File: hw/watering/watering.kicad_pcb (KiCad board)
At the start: 2 copper layers, 57 x 57 mm, 51 parts, among them J2 USB_C_Receptacle, SW1 KMS221GLFS, SW2 KMS221GLFS, U1 ESP32-C6, U2 DRV8220DSG, U3 NCP163AFCT330T2G, U4 STI3508, U5 STI3508, U6 STI3508, Y1 40MHz, Y2 32768Hz

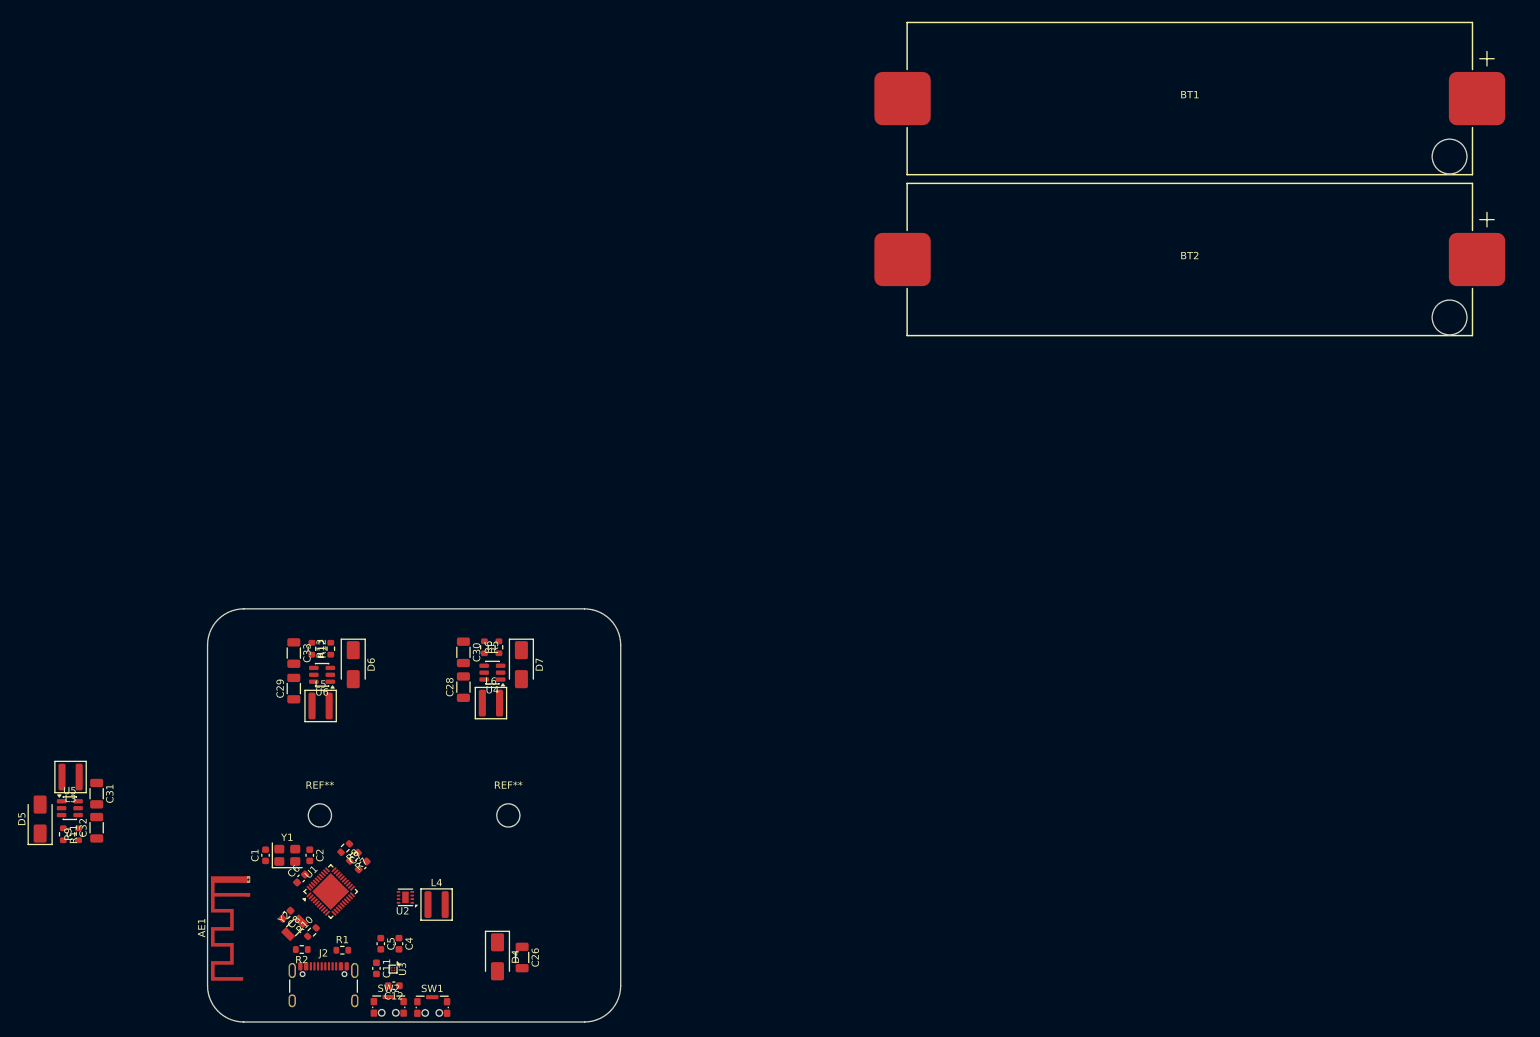
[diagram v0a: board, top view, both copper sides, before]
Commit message: connections completet. started placing and routing
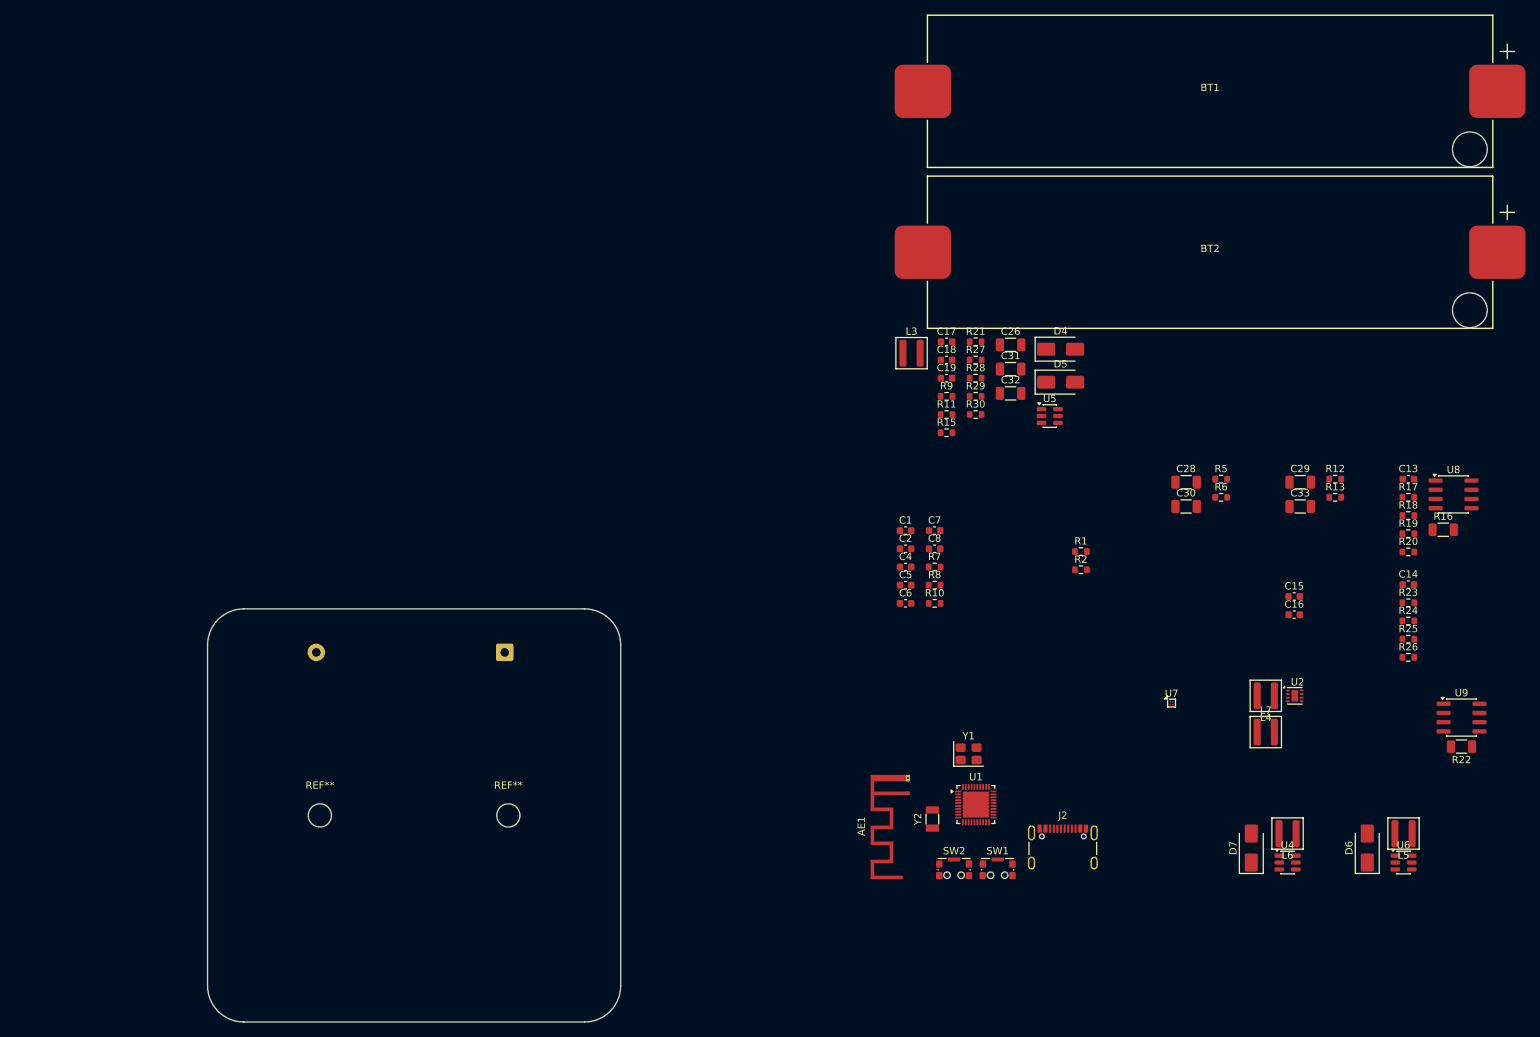
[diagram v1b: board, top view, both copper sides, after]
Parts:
- removed C11, C12: 1u, Capacitor_SMD:C_0603_1608Metric
- removed U3: NCP163AFCT330T2G, Package_CSP:WLCSP-4_0.64x0.64mm_Layout2x2_P0.35mm
- added C13: 1u, Capacitor_SMD:C_0603_1608Metric, F.Cu at (265.7, 82.1)
- added C14: 1u, Capacitor_SMD:C_0603_1608Metric, F.Cu at (265.7, 96.7)
- added C15: 1u, Capacitor_SMD:C_0603_1608Metric, F.Cu at (249.9, 98.3)
- added C16: 1u, Capacitor_SMD:C_0603_1608Metric, F.Cu at (249.9, 100.8)
- added C17: 1u, Capacitor_SMD:C_0603_1608Metric, F.Cu at (202.0, 63.2)
- added C18: 1u, Capacitor_SMD:C_0603_1608Metric, F.Cu at (202.0, 65.7)
- added C19: 1u, Capacitor_SMD:C_0603_1608Metric, F.Cu at (202.0, 68.2)
- added L7: 22u, Inductor_SMD:L_Wuerth_MAPI-4030, F.Cu at (246.0, 117.0)
- added R15: 10k, Resistor_SMD:R_0603_1608Metric, F.Cu at (202.0, 75.7)
- added R16: 0R1, Resistor_SMD:R_1206_3216Metric, F.Cu at (270.5, 89.1)
- added R17: 10k, Resistor_SMD:R_0603_1608Metric, F.Cu at (265.7, 84.6)
- added R18: 10k, Resistor_SMD:R_0603_1608Metric, F.Cu at (265.7, 87.1)
- added R19: 100k, Resistor_SMD:R_0603_1608Metric, F.Cu at (265.7, 89.6)
- added R20: 10k, Resistor_SMD:R_0603_1608Metric, F.Cu at (265.7, 92.1)
- added R21: 39k, Resistor_SMD:R_0603_1608Metric, F.Cu at (206.0, 63.2)
- added R22: 0R1, Resistor_SMD:R_1206_3216Metric, F.Cu at (273.0, 119.0)
- added R23: 10k, Resistor_SMD:R_0603_1608Metric, F.Cu at (265.7, 99.2)
- added R24: 10k, Resistor_SMD:R_0603_1608Metric, F.Cu at (265.7, 101.7)
- added R25: 10k, Resistor_SMD:R_0603_1608Metric, F.Cu at (265.7, 104.2)
- added R26: 100k, Resistor_SMD:R_0603_1608Metric, F.Cu at (265.7, 106.7)
- added R27: 220k, Resistor_SMD:R_0603_1608Metric, F.Cu at (206.0, 65.7)
- added R28: 10k, Resistor_SMD:R_0603_1608Metric, F.Cu at (206.0, 68.2)
- added R29: 47k, Resistor_SMD:R_0603_1608Metric, F.Cu at (206.0, 70.7)
- added R30: 10k, Resistor_SMD:R_0603_1608Metric, F.Cu at (206.0, 73.2)
- added SC1: Solar_Cell, Capacitor_THT:CP_Axial_L20.0mm_D10.0mm_P26.00mm_Horizontal, B.Cu at (141.0, 106.0)
- added U7: NCP163AFCT330T2G, Package_CSP:WLCSP-4_0.64x0.64mm_Layout2x2_P0.35mm, F.Cu at (233.0, 113.0)
- added U8: MCP6002-xSN, Package_SO:SOIC-8_3.9x4.9mm_P1.27mm, F.Cu at (271.9, 84.2)
- added U9: MCP6002-xSN, Package_SO:SOIC-8_3.9x4.9mm_P1.27mm, F.Cu at (273.0, 115.0)
- moved D5 153.1 mm to (217.7, 68.7), turned to 0 degrees
- moved U6 151.4 mm to (265.0, 135.0), turned to 0 degrees
- moved L5 150.4 mm to (265.0, 131.0), turned to 180 degrees
- moved U5 145.6 mm to (216.2, 73.4)
- moved R12 143.1 mm to (255.6, 82.1), turned to 0 degrees
- moved D6 142.2 mm to (260.0, 133.0), turned to 90 degrees
- moved C29 141.7 mm to (250.7, 82.5), turned to 0 degrees
- moved C33 140.3 mm to (250.7, 85.9), turned to 0 degrees
- moved R13 140.1 mm to (255.6, 84.6), turned to 0 degrees
- moved C32 139.6 mm to (210.8, 70.3), turned to 0 degrees
- moved C31 139.0 mm to (210.8, 66.9), turned to 0 degrees
- moved R11 134.9 mm to (202.0, 73.2), turned to 0 degrees
- moved R9 134.1 mm to (202.0, 70.7), turned to 0 degrees
- moved L3 129.9 mm to (197.1, 64.7), turned to 0 degrees
- moved U2 125.8 mm to (250.0, 112.0), turned to 0 degrees
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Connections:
- net /controller/bat_interrupt renamed /controller/i_usb_meas
- L4 pad 2: /solar/V_bat -> /solar/current_meas/i_in
- U1 pad 10: unconnected-(U1-MTMS/GPIO4/FSPIHD/ADC1_CH4-Pad10) -> /controller/V_solar_meas
- U1 pad 11: unconnected-(U1-MTDI/GPIO5/FSPIWP/ADC1_CH5-Pad11) -> /controller/V_usb_meas
- U1 pad 12: unconnected-(U1-MTCK/GPIO6/FSPICLK/ADC1_CH6-Pad12) -> /controller/V_bat_meas
- U1 pad 14: unconnected-(U1-GPIO8-Pad14) -> /controller/pwm-enable
- U1 pad 15: unconnected-(U1-GPIO9-Pad15) -> /controller/usb-pwm
- U1 pad 16: unconnected-(U1-GPIO10-Pad16) -> /controller/solar-pwm
- U1 pad 9: unconnected-(U1-GPIO3/ADC1_CH3-Pad9) -> /controller/i_meas_solar
- U2 pad 3: Net-(U2-OUT1) -> Net-(U2-OUT2)
- U2 pad 5: /solar/solar_pwm -> /controller/usb-pwm
- U2 pad 6: /solar/solar_pwm -> /controller/solar-pwm
- U2 pad 8: /solar/solar_enable -> /controller/pwm-enable
- U4 pad 4: /controller/v2 -> /controller/v1
- U5 pad 4: /solar/v_en -> /solar/V_bat
- U6 pad 4: /controller/v1 -> /controller/v2

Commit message: some more placing
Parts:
- removed C8: 100n, Capacitor_SMD:C_0603_1608Metric
- removed R7, R8: 10k, Resistor_SMD:R_0603_1608Metric
- moved U9 150.7 mm to (122.5, 107.0), turned to 90 degrees
- moved C14 147.1 mm to (118.8, 104.8), turned to -90 degrees
- moved R22 147.1 mm to (126.5, 105.5), turned to -90 degrees
- moved R25 147.0 mm to (118.8, 109.2), turned to 90 degrees
- moved R24 146.5 mm to (119.5, 112.0), turned to 180 degrees
- moved C15 146.4 mm to (104.0, 110.2), turned to -90 degrees
- moved R23 142.7 mm to (123.5, 112.0), turned to 180 degrees
- moved R26 141.2 mm to (124.5, 102.2), turned to 180 degrees
- moved R16 140.6 mm to (131.5, 110.2), turned to -90 degrees
- moved U8 138.3 mm to (135.4, 107.0), turned to -90 degrees
- moved R19 132.3 mm to (135.2, 111.8)
- moved R18 132.0 mm to (134.5, 102.2)
- moved C13 129.5 mm to (139.0, 109.2), turned to 90 degrees
- moved R21 128.7 mm to (111.2, 150.2), turned to 180 degrees
- moved R17 128.6 mm to (138.2, 102.2)
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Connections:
- U5 pad 1: (no net) -> Net-(D5-A)

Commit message: routing done
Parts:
- removed C4: 100n, Capacitor_SMD:C_0603_1608Metric
- added C20: 1u, Capacitor_SMD:C_0603_1608Metric, F.Cu at (122.1, 148.3)
- added C21: 1u, Capacitor_SMD:C_0603_1608Metric, F.Cu at (223.6, 129.8)
- added C24: 1u, Capacitor_SMD:C_0603_1608Metric, F.Cu at (226.8, 121.3)
- added C27: 22u, Capacitor_SMD:C_1206_3216Metric, F.Cu at (153.8, 108.5)
- added C34: 22u, Capacitor_SMD:C_1206_3216Metric, F.Cu at (224.0, 123.0)
- added C35: 22u, Capacitor_SMD:C_1206_3216Metric, F.Cu at (228.0, 133.0)
- added C36: 22u, Capacitor_SMD:C_1206_3216Metric, F.Cu at (153.8, 111.0)
- added D1: SMBJ6.5CA, Diode_SMD:D_SMB, F.Cu at (136.0, 138.8)
- added D2: SMBJ6.5CA, Diode_SMD:D_SMB, F.Cu at (143.5, 138.8)
- added D8: SS210, Diode_SMD:D_SMA, F.Cu at (216.0, 120.8)
- added J3: Conn_01x02_Pin, DORABO:DB142R-5.08-2P-GN, F.Cu at (241.4, 141.4)
- added J4: Conn_01x02_Pin, DORABO:DB142R-5.08-2P-GN, F.Cu at (255.4, 141.4)
- added J6: Conn_01x02_Pin, DORABO:DB142R-5.08-2P-GN, F.Cu at (222.0, 141.5)
- added L8: 22u, Inductor_SMD:L_Wuerth_MAPI-4030, F.Cu at (220.2, 123.0)
- added Q1: 2N7002, Package_TO_SOT_SMD:SOT-23, F.Cu at (227.9, 118.8)
- added R14: 10k, Resistor_SMD:R_0603_1608Metric, F.Cu at (183.7, 133.6)
- added R31: 10k, Resistor_SMD:R_0603_1608Metric, F.Cu at (194.8, 131.1)
- added R32: 10k, Resistor_SMD:R_0603_1608Metric, F.Cu at (183.7, 125.2)
- added R33: 47, Resistor_SMD:R_0603_1608Metric, F.Cu at (194.8, 128.1)
- added R34: 47, Resistor_SMD:R_0603_1608Metric, F.Cu at (194.8, 129.6)
- added R35: 10k, Resistor_SMD:R_0603_1608Metric, F.Cu at (194.8, 132.7)
- added R36: 0R1, Resistor_SMD:R_1206_3216Metric, F.Cu at (225.5, 133.0)
- added R37: 10k, Resistor_SMD:R_0603_1608Metric, F.Cu at (213.5, 134.5)
- added R38: 10k, Resistor_SMD:R_0603_1608Metric, F.Cu at (213.5, 131.2)
- added R39: 10k, Resistor_SMD:R_0603_1608Metric, F.Cu at (218.2, 128.8)
- added R40: 100k, Resistor_SMD:R_0603_1608Metric, F.Cu at (223.0, 132.5)
- added R41: 1k, Resistor_SMD:R_0603_1608Metric, F.Cu at (223.2, 118.8)
- added R42: 1k, Resistor_SMD:R_0603_1608Metric, F.Cu at (225.3, 116.4)
- added R43: 10k, Resistor_SMD:R_0603_1608Metric, F.Cu at (225.0, 118.8)
- added U10: MCP6002-xSN, Package_SO:SOIC-8_3.9x4.9mm_P1.27mm, F.Cu at (218.2, 132.5)
- added U11: STI3508, Package_TO_SOT_SMD:SOT-23-6, F.Cu at (220.2, 118.7)
- added U3: W25Q128JVS, Package_SO:SOIC-8_5.3x5.3mm_P1.27mm, F.Cu at (193.3, 124.3)
- SC1: footprint Capacitor_THT:CP_Axial_L20.0mm_D10.0mm_P26.00mm_Horizontal -> DORABO:DB142R-5.08-2P-GN; moved to F.Cu
- moved BT1 192.8 mm to (65.0, 113.0)
- moved BT2 192.7 mm to (65.0, 135.0)
- moved REF** 130.5 mm to (272.0, 125.0)
- moved C29 123.7 mm to (259.5, 128.2), turned to -90 degrees
- moved C33 123.6 mm to (259.5, 133.0), turned to 90 degrees
- moved D6 121.2 mm to (256.2, 131.8)
- moved C28 119.9 mm to (245.2, 128.2), turned to -90 degrees
- moved C30 119.8 mm to (245.2, 133.0), turned to 90 degrees
- moved D7 117.6 mm to (242.0, 131.8)
- moved U6 112.5 mm to (252.2, 132.5), turned to -90 degrees
- moved L5 112.4 mm to (252.0, 127.8), turned to -90 degrees
- moved U4 109.0 mm to (238.0, 132.2), turned to -90 degrees
- moved L6 108.9 mm to (237.8, 127.5), turned to -90 degrees
- moved R12 108.6 mm to (249.5, 131.8), turned to 90 degrees
- moved R13 108.1 mm to (249.0, 134.5)
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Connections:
- net Net-(AE1-A) renamed /controller/antenna
- C19 pad 1: /controller/V_usb_meas -> /V_usb_avail
- R10 pad 2: /controller/i_usb_meas -> /controller/SDA
- R29 pad 1: /controller/V_usb_meas -> /V_usb_avail
- R30 pad 1: /controller/V_usb_meas -> /V_usb_avail
- U1 pad 11: /controller/V_usb_meas -> /conductivity/i_cond_meas
- U1 pad 14: /controller/pwm-enable -> Net-(U1-GPIO8)
- U1 pad 15: /controller/usb-pwm -> /controller/boot
- U1 pad 16: /controller/solar-pwm -> unconnected-(U1-GPIO10-Pad16)
- U1 pad 18: /controller/USBDM -> Net-(U1-GPIO12/USB_D-)
- U1 pad 19: /controller/USBDP -> Net-(U1-GPIO13/USB_D+)
- U1 pad 20: unconnected-(U1-SPICS0/GPIO24-Pad20) -> Net-(U1-SPICS0/GPIO24)
- U1 pad 21: unconnected-(U1-SPIQ/GPIO25-Pad21) -> Net-(U1-SPIQ/GPIO25)
- U1 pad 22: unconnected-(U1-SPIWP/GPIO26-Pad22) -> Net-(U1-SPIWP/GPIO26)
- U1 pad 23: unconnected-(U1-VDD_SPI/GPIO27-Pad23) -> Net-(U1-VDD_SPI/GPIO27)
- U1 pad 24: unconnected-(U1-SPIHD/GPIO28-Pad24) -> Net-(U1-SPIHD/GPIO28)
- U1 pad 25: unconnected-(U1-SPICLK/GPIO29-Pad25) -> Net-(U1-SPICLK/GPIO29)
- U1 pad 26: unconnected-(U1-SPID/GPIO30-Pad26) -> Net-(U1-SPID/GPIO30)
- U1 pad 31: unconnected-(U1-GPIO18/SDIO_CMD/FSPICS2-Pad31) -> /controller/usb-pwm
- U1 pad 32: unconnected-(U1-GPIO19/SDIO_CLK/FSPICS3-Pad32) -> /controller/pwm-enable
- U1 pad 33: unconnected-(U1-GPIO20/SDIO_DATA0/FSPICS4-Pad33) -> /controller/solar-pwm
- U1 pad 34: unconnected-(U1-GPIO21/SDIO_DATA1/FSPICS5-Pad34) -> /V_usb_avail
- U1 pad 35: unconnected-(U1-GPIO22/SDIO_DATA2-Pad35) -> /conductivity/cond_pwm
- U1 pad 36: unconnected-(U1-GPIO23/SDIO_DATA3-Pad36) -> /conductivity/v_en
- U1 pad 6: /controller/boot -> Net-(U1-GPIO0/XTAL_32K_P/ADC1_CH0)
- Y2 pad 1: /controller/boot -> Net-(U1-GPIO0/XTAL_32K_P/ADC1_CH0)
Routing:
- net /GND: track 0.00 -> 424.3 mm, vias 0 -> 36
- net /+3V3: track 0.00 -> 297.6 mm, vias 0 -> 24
- net /+5V: track 0.00 -> 113.7 mm, vias 0 -> 4
- net /controller/boot: track 0.00 -> 103.1 mm, vias 0 -> 2
- net /controller/V_bat_meas: track 0.00 -> 99.2 mm, vias 0 -> 4
- net /controller/reset: track 0.00 -> 90.4 mm, vias 0 -> 3
- net /controller/i_meas_solar: track 0.00 -> 82.4 mm, vias 0 -> 2
- net /controller/i_usb_meas: track 0.00 -> 79.7 mm, vias 0 -> 2
- net /solar/V_bat: track 0.00 -> 77.7 mm, vias 0 -> 7
- net /solar/+Vsolar: track 0.00 -> 75.2 mm, vias 0 -> 1
- net /controller/USBDP: track 0.00 -> 74.6 mm, vias 0 -> 4
- net /controller/pwm-enable: track 0.00 -> 72.1 mm, vias 0 -> 2
- net /controller/USBDM: track 0.00 -> 70.7 mm, vias 0 -> 2
- net /controller/solar-pwm: track 0.00 -> 70.1 mm, vias 0 -> 2
- net /controller/usb-pwm: track 0.00 -> 68.1 mm, vias 0 -> 2
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- added copper zone on B.Cu, net /GND
- added copper zone on F.Cu, net /GND
- added copper zone on F.Cu, net /controller/antenna
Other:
- board size 57 x 57 mm -> 262 x 50 mm

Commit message: - updated parts numbers - created jlc outputs
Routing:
- net /GND: track 424.3 -> 427.5 mm, vias 36 -> 60

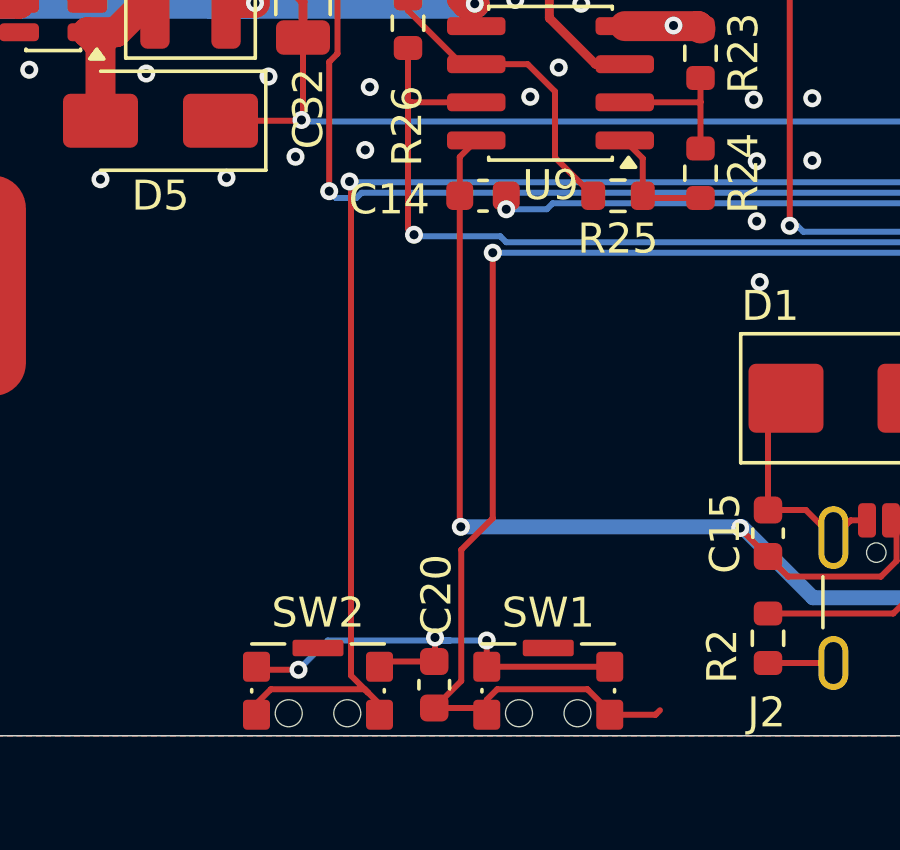
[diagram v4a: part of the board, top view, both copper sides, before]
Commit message: updated switches
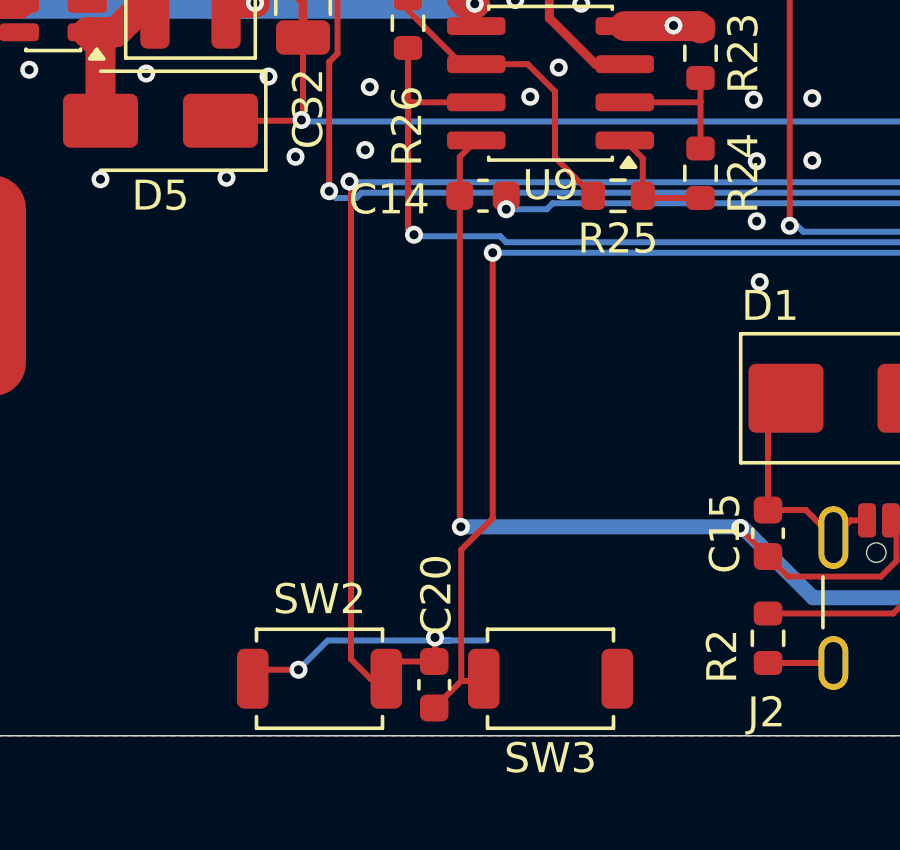
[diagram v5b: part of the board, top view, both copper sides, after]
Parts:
- removed SW1: KMS221GLFS, Button_Switch_SMD:SW_SPST_CK_KMS2xxGP
- added SW3: KMS221GLFS, Button_Switch_SMD:SW_SPST_TS-1088-xR020, F.Cu at (126.0, 148.1)
- SW2: footprint Button_Switch_SMD:SW_SPST_CK_KMS2xxGP -> Button_Switch_SMD:SW_SPST_TS-1088-xR020
- moved SW2 0.40 mm to (118.3, 148.1)
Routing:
- net /controller/reset: track 90.4 -> 82.4 mm
- net /controller/boot: track 103.1 -> 98.0 mm
- net /GND: track 427.5 -> 422.6 mm, vias 60 -> 59
